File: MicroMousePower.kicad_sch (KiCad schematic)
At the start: 12 parts, among them Q1 NPN, U1 INA219AxDCN, U2 MCP73831-3-MC

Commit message: MEOW?
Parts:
- removed Q1: NPN, symbol Simulation_SPICE:NPN
- added T1: TIP31C, symbol TIP31C:TIP31C
- added TP1, TP2, TP3: TestPoint, symbol Connector:TestPoint
- renumbered Battery to Battery1
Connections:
- net +9V: now also T1.2, TP3.1
- net at Battery1.1, R2.1: now also T1.3, TP2.1
- net at R3.2: now also T1.1, TP1.1
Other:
- note added: "HEEEEEEEEELLLLLLLLLLLOOOOOOOOOOOOOOOOOOOOOOO"
- note added: "charging current for the battery (200mA or 600mA ±100mA)"
- note removed: "higher and lower charging current for the battery (200mA or 600mA ±100mA)"
- moved on the sheet: Battery1, R2, R3

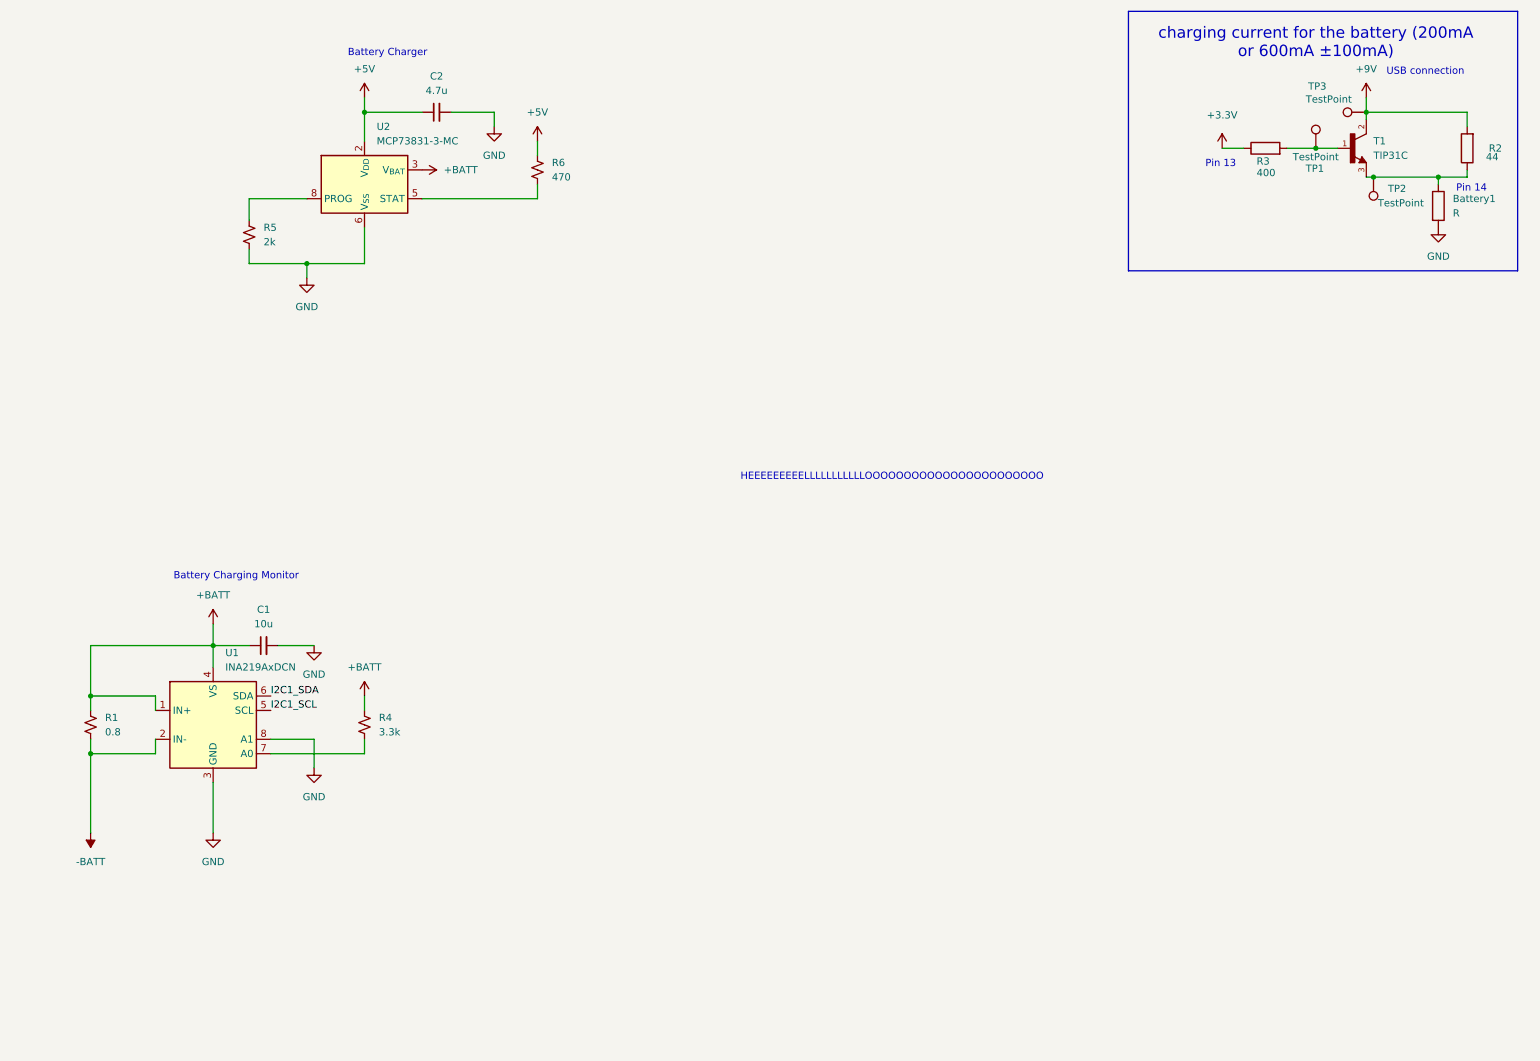
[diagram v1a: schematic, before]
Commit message: organized circuit sections, added schematic metadata
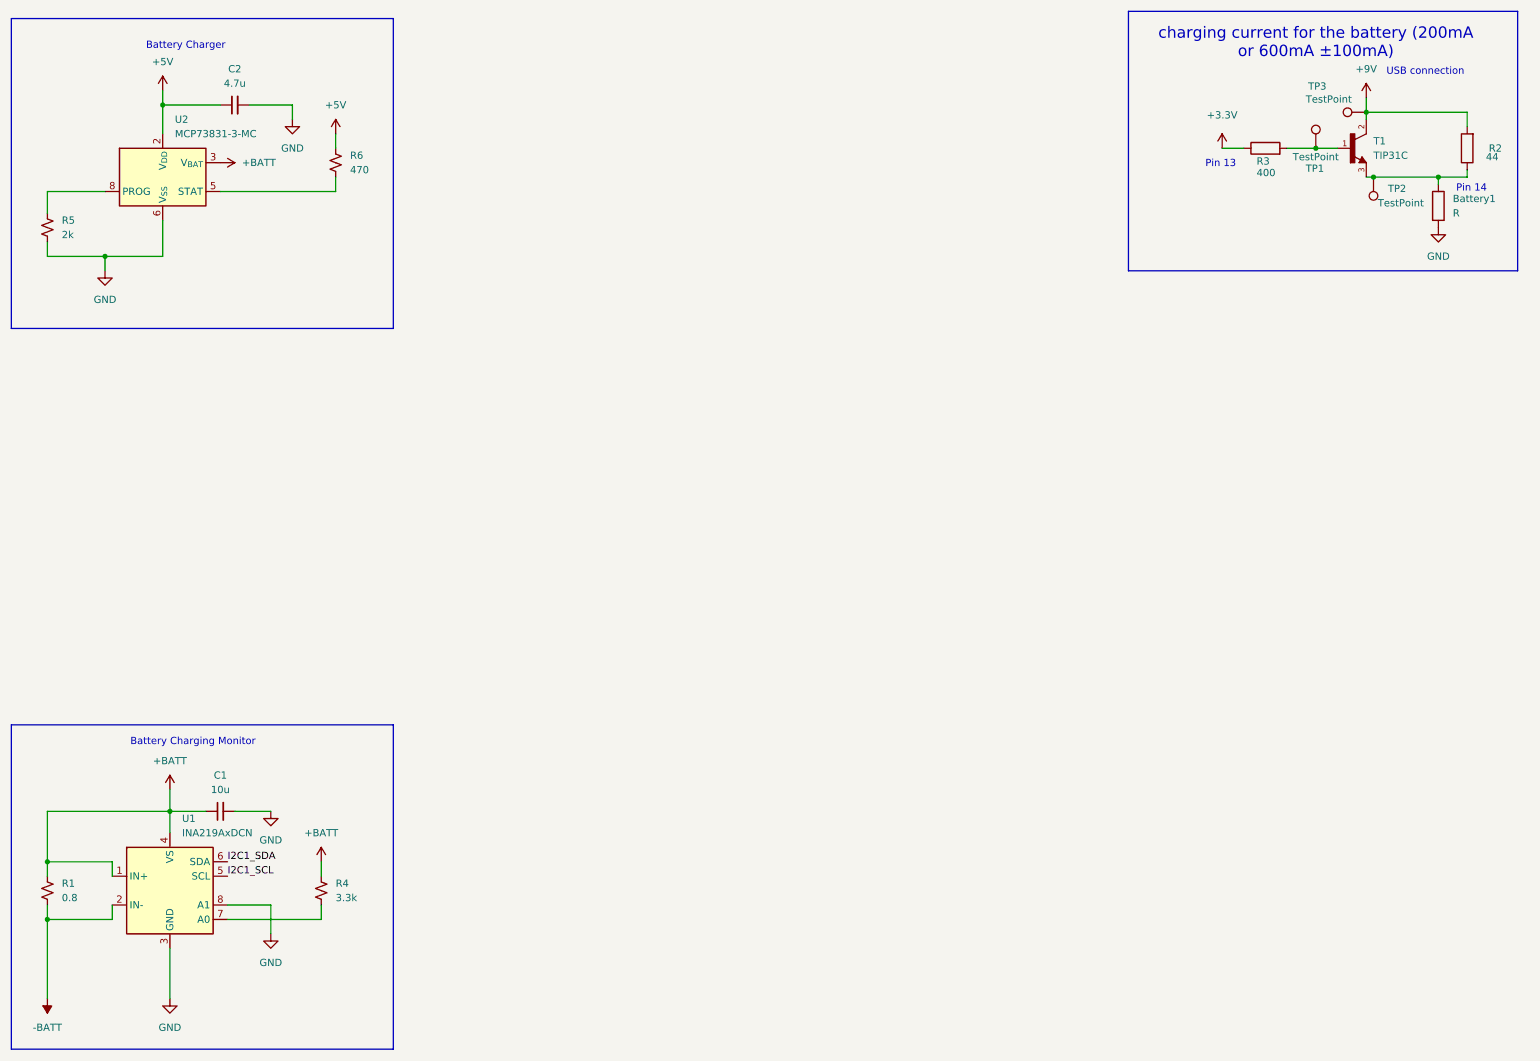
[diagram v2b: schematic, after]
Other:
- note removed: "HEEEEEEEEELLLLLLLLLLLOOOOOOOOOOOOOOOOOOOOOOO"
- company: (none) -> University of Cape Town
- title: (none) -> MicroMouse Power Subsystem Design
- moved on the sheet: C1, C2, R1, R4, R5, R6, U1, U2

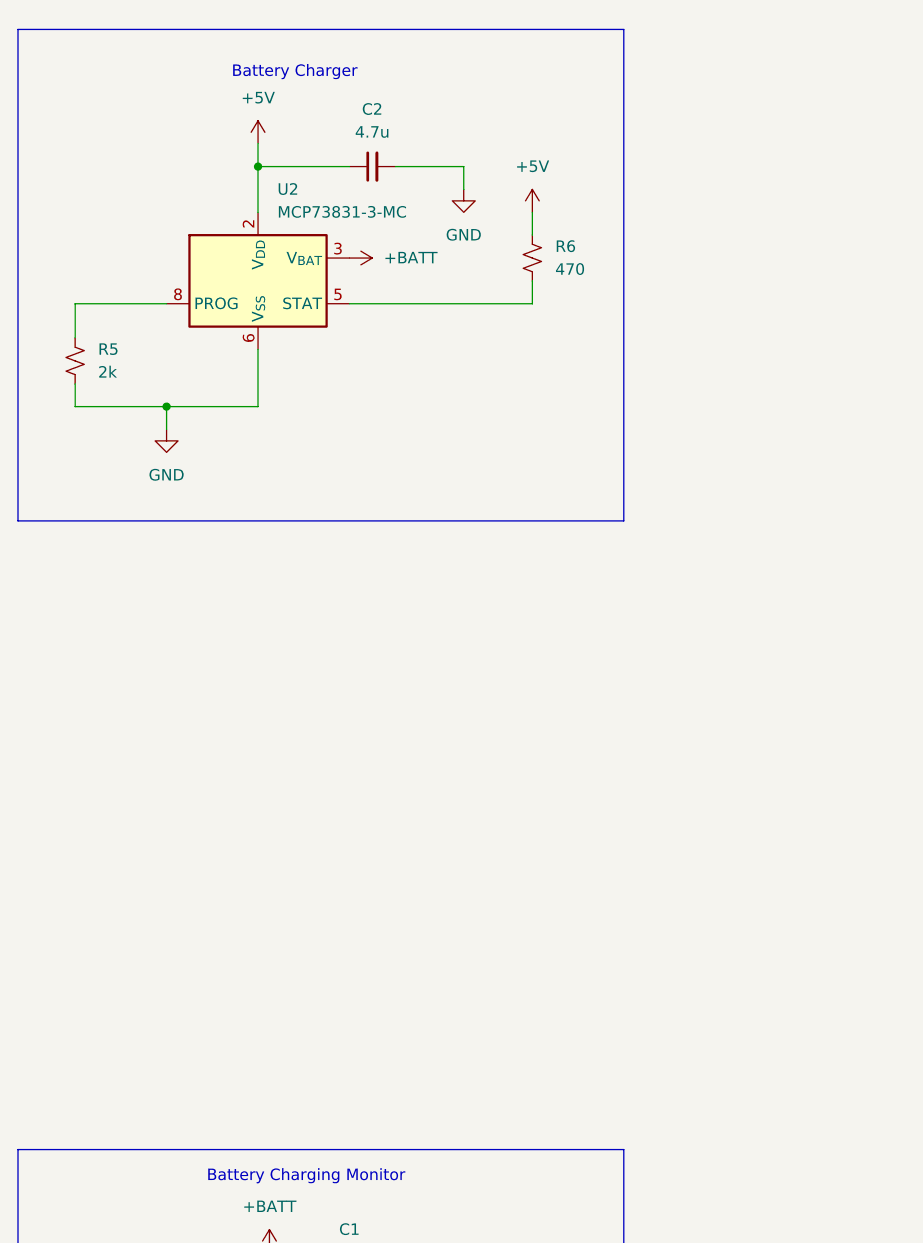
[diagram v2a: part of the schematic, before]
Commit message: integrated USB C 9V negotiator
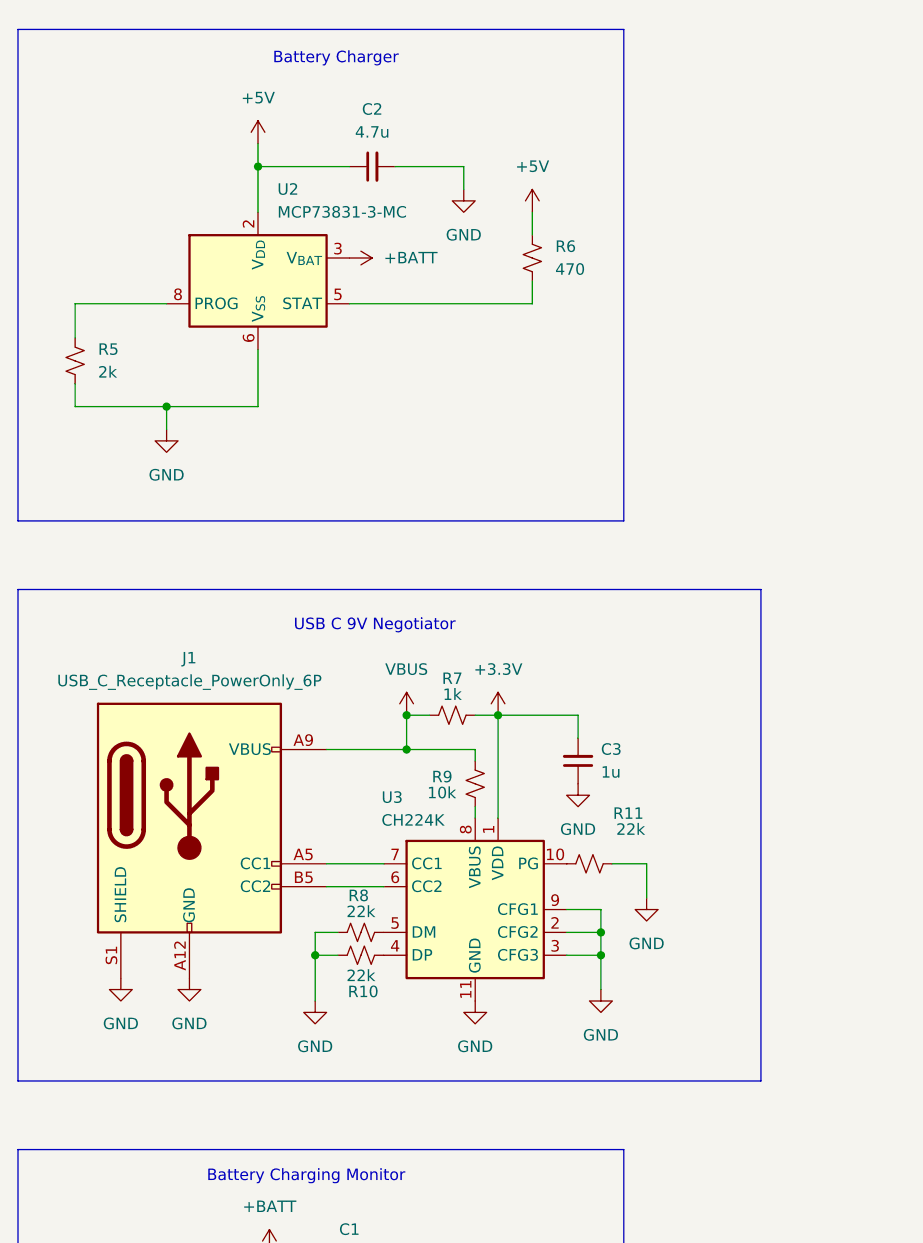
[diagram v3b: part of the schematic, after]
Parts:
- added C3: 1u, symbol Device:C_Small
- added J1: USB_C_Receptacle_PowerOnly_6P, symbol Connector:USB_C_Receptacle_PowerOnly_6P
- added R10, R11, R8: 22k, symbol Device:R_Small_US
- added R7: 1k, symbol Device:R_Small_US
- added R9: 10k, symbol Device:R_Small_US
- added U3: CH224K, Package_SO:SSOP-10-1EP_3.9x4.9mm_P1mm_EP2.1x3.3mm, symbol Interface_USB:CH224K
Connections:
- net +3.3V: now also C3.2, R7.2, U3.1 (VDD)
- net GND: now also C3.1, J1.A12 (GND), J1.B12 (GND), J1.S1 (SHIELD), R10.2, R11.2, R8.1, U3.11 (GND), U3.2 (CFG2), U3.3 (CFG3), U3.9 (CFG1)
- new net: R11.1, U3.10 (PG)
- new net: R10.1, U3.4 (DP)
- new net: R8.2, U3.5 (DM)
- new net: J1.B5 (CC2), U3.6 (CC2)
- new net: J1.A5 (CC1), U3.7 (CC1)
- new net: R9.2, U3.8 (VBUS)
- new net VBUS: J1.A9 (VBUS), J1.B9 (VBUS), R7.1, R9.1
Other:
- note added: "USB C 9V Negotiator"

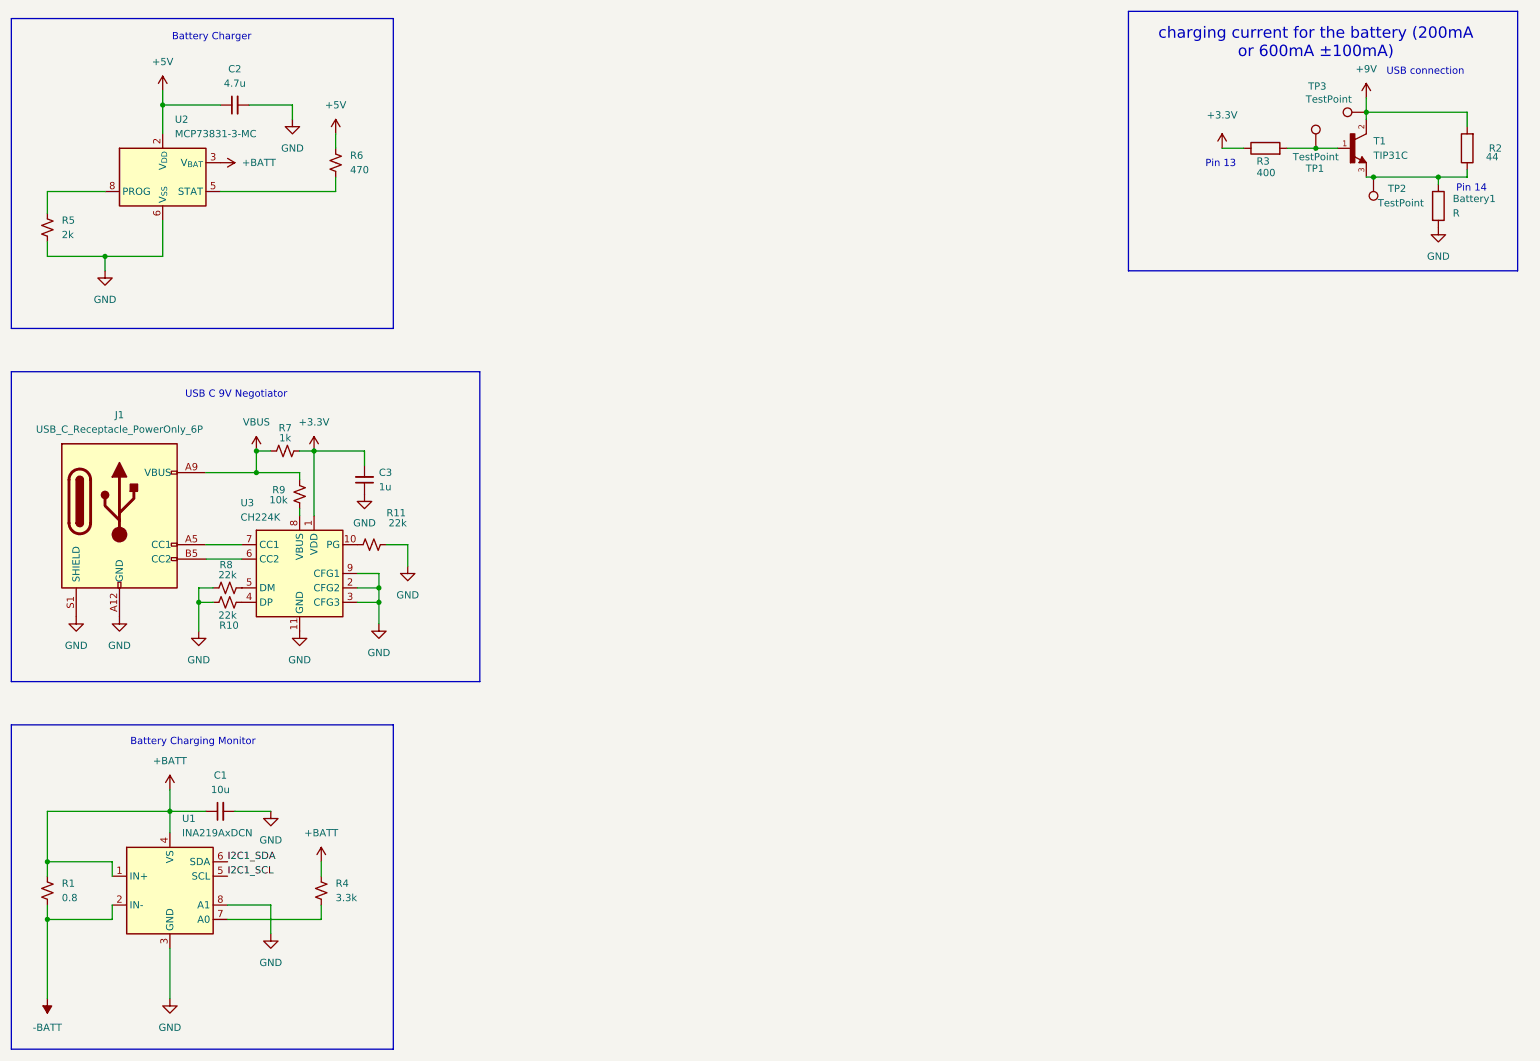
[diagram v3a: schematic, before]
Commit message: defined motherboard interface and added motor driver IC
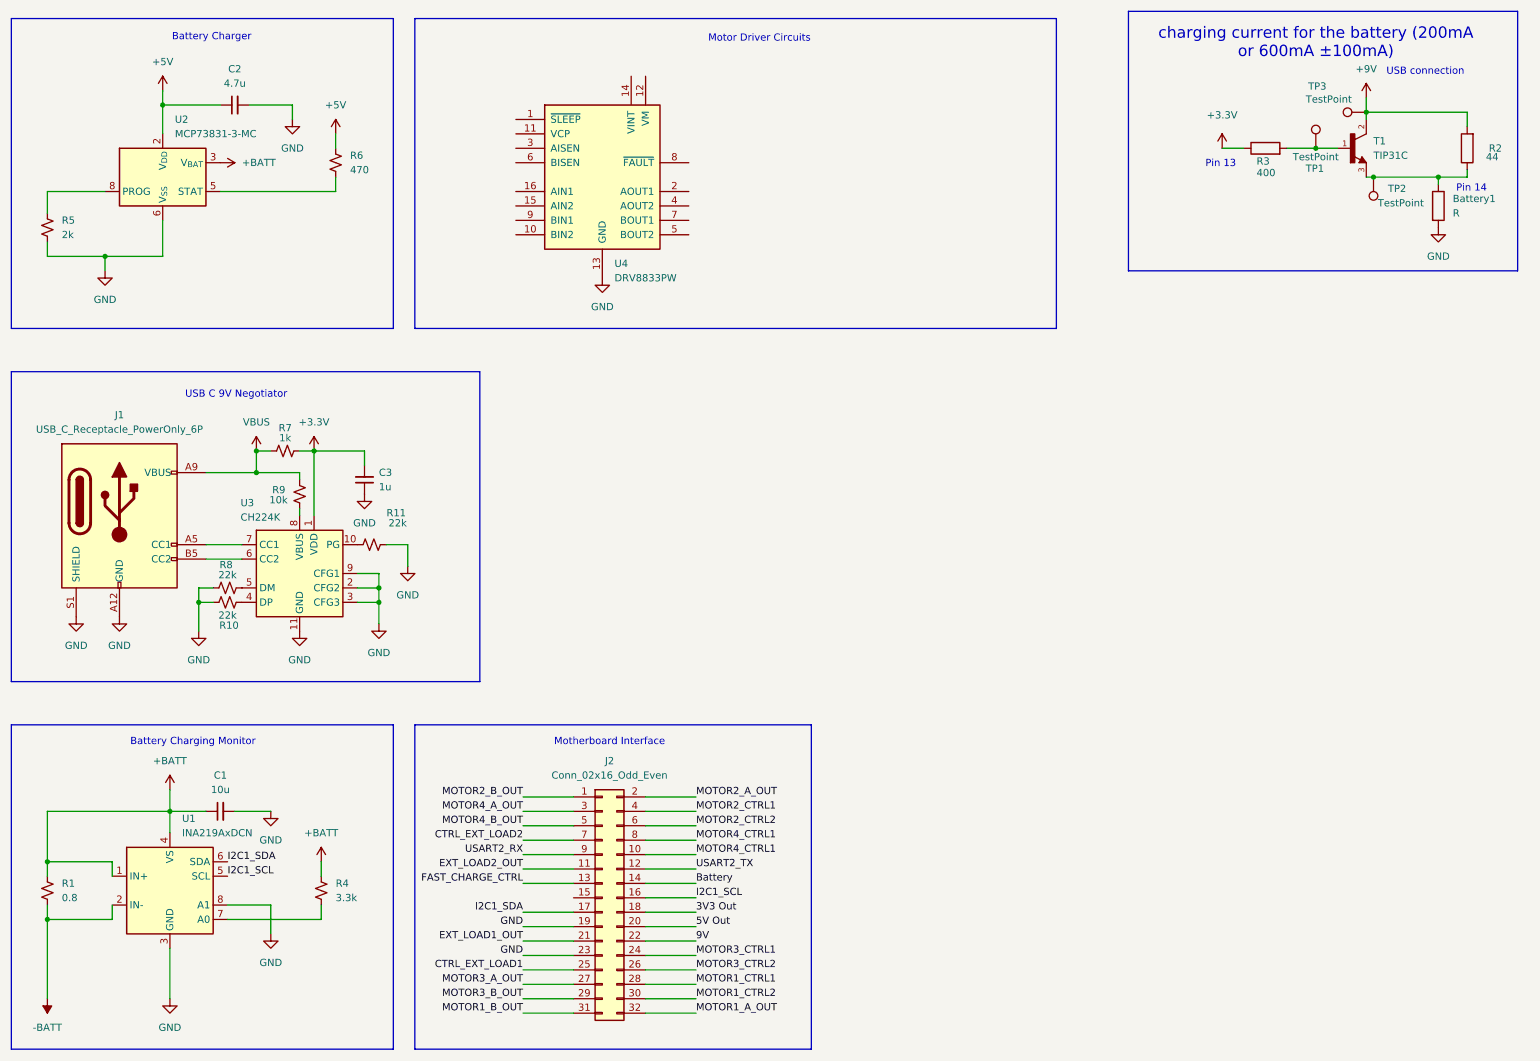
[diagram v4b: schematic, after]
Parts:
- added J2: Conn_02x16_Odd_Even, symbol Connector_Generic:Conn_02x16_Odd_Even
- added U4: DRV8833PW, Package_SO:TSSOP-16_4.4x5mm_P0.65mm, symbol Driver_Motor:DRV8833PW
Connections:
- net GND: now also J2.19 (Pin_19), J2.23 (Pin_23), U4.13 (GND)
- net I2C1_SCL: now also J2.16 (Pin_16)
- net I2C1_SDA: now also J2.17 (Pin_17)
- new net 3V3 Out: J2.18 (Pin_18)
- new net 5V Out: J2.20 (Pin_20)
- new net 9V: J2.22 (Pin_22)
- new net Battery: J2.14 (Pin_14)
- new net CTRL_EXT_LOAD1: J2.25 (Pin_25)
- new net CTRL_EXT_LOAD2: J2.7 (Pin_7)
- new net EXT_LOAD1_OUT: J2.21 (Pin_21)
- new net EXT_LOAD2_OUT: J2.11 (Pin_11)
- new net FAST_CHARGE_CTRL: J2.13 (Pin_13)
- new net MOTOR1_A_OUT: J2.32 (Pin_32)
- new net MOTOR1_B_OUT: J2.31 (Pin_31)
- new net MOTOR1_CTRL1: J2.28 (Pin_28)
- new net MOTOR1_CTRL2: J2.30 (Pin_30)
- new net MOTOR2_A_OUT: J2.2 (Pin_2)
- new net MOTOR2_B_OUT: J2.1 (Pin_1)
- new net MOTOR2_CTRL1: J2.4 (Pin_4)
- new net MOTOR2_CTRL2: J2.6 (Pin_6)
- new net MOTOR3_A_OUT: J2.27 (Pin_27)
- new net MOTOR3_B_OUT: J2.29 (Pin_29)
- new net MOTOR3_CTRL1: J2.24 (Pin_24)
- new net MOTOR3_CTRL2: J2.26 (Pin_26)
- new net MOTOR4_A_OUT: J2.3 (Pin_3)
- new net MOTOR4_B_OUT: J2.5 (Pin_5)
- new net MOTOR4_CTRL1: J2.10 (Pin_10), J2.8 (Pin_8)
- new net USART2_RX: J2.9 (Pin_9)
- new net USART2_TX: J2.12 (Pin_12)
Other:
- note added: "Motherboard Interface"
- note added: "Motor Driver Circuits"
